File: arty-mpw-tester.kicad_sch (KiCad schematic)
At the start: 111 parts, among them J1 USB4105-GF-A, J10 61300211121, J11 61300211121, J12 61300211121, J14 61300311121, J15 61300311121, J18 61300411121, J19 61300711121, J20 61300411121, J3 arty_chipKIT_connector, J4 61300211121, J5 61300311121, J6 61300211121, J7 61300211121, J8 61300211121, J9 61300211121, Q1 DTC014TEBTL, SW1 JS202011JCQN, SW3 JS202011JCQN, U1 TAR5S33UTE85LF, U10 TPD4E02B04DQA, U2 FT4232H-56Q, U4 MAX811REUS+T, U5 NTS0102DP, U6 MCP4661-103E/ML, U7 Caravel_breakout_PCB_flexypin, U8 W25Q32FVSS, U9 MIC2211-AAYML-TR, Y1 ABM8G-12.000MHZ-18-D2Y-T, Y2 ECS-2520MVLC-100-BN-TR

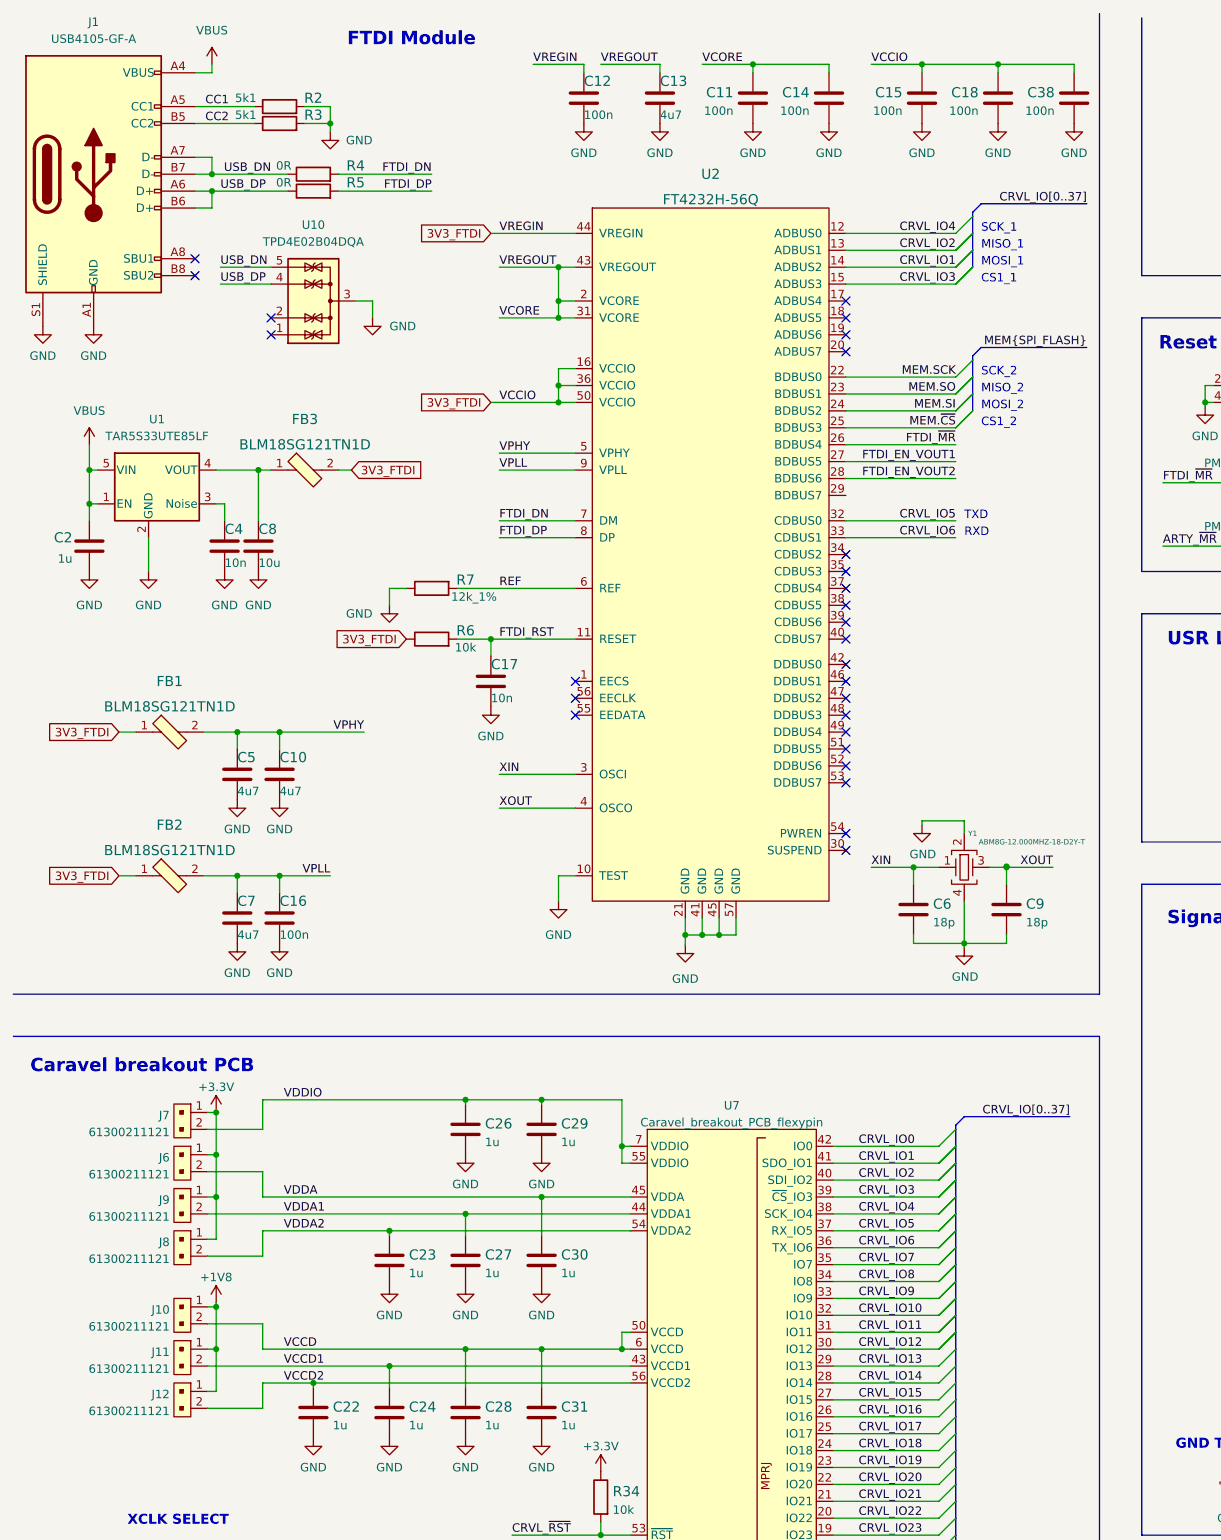
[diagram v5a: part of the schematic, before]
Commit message: Added current monitor schematics. Moved FTDI module to separate subsheet
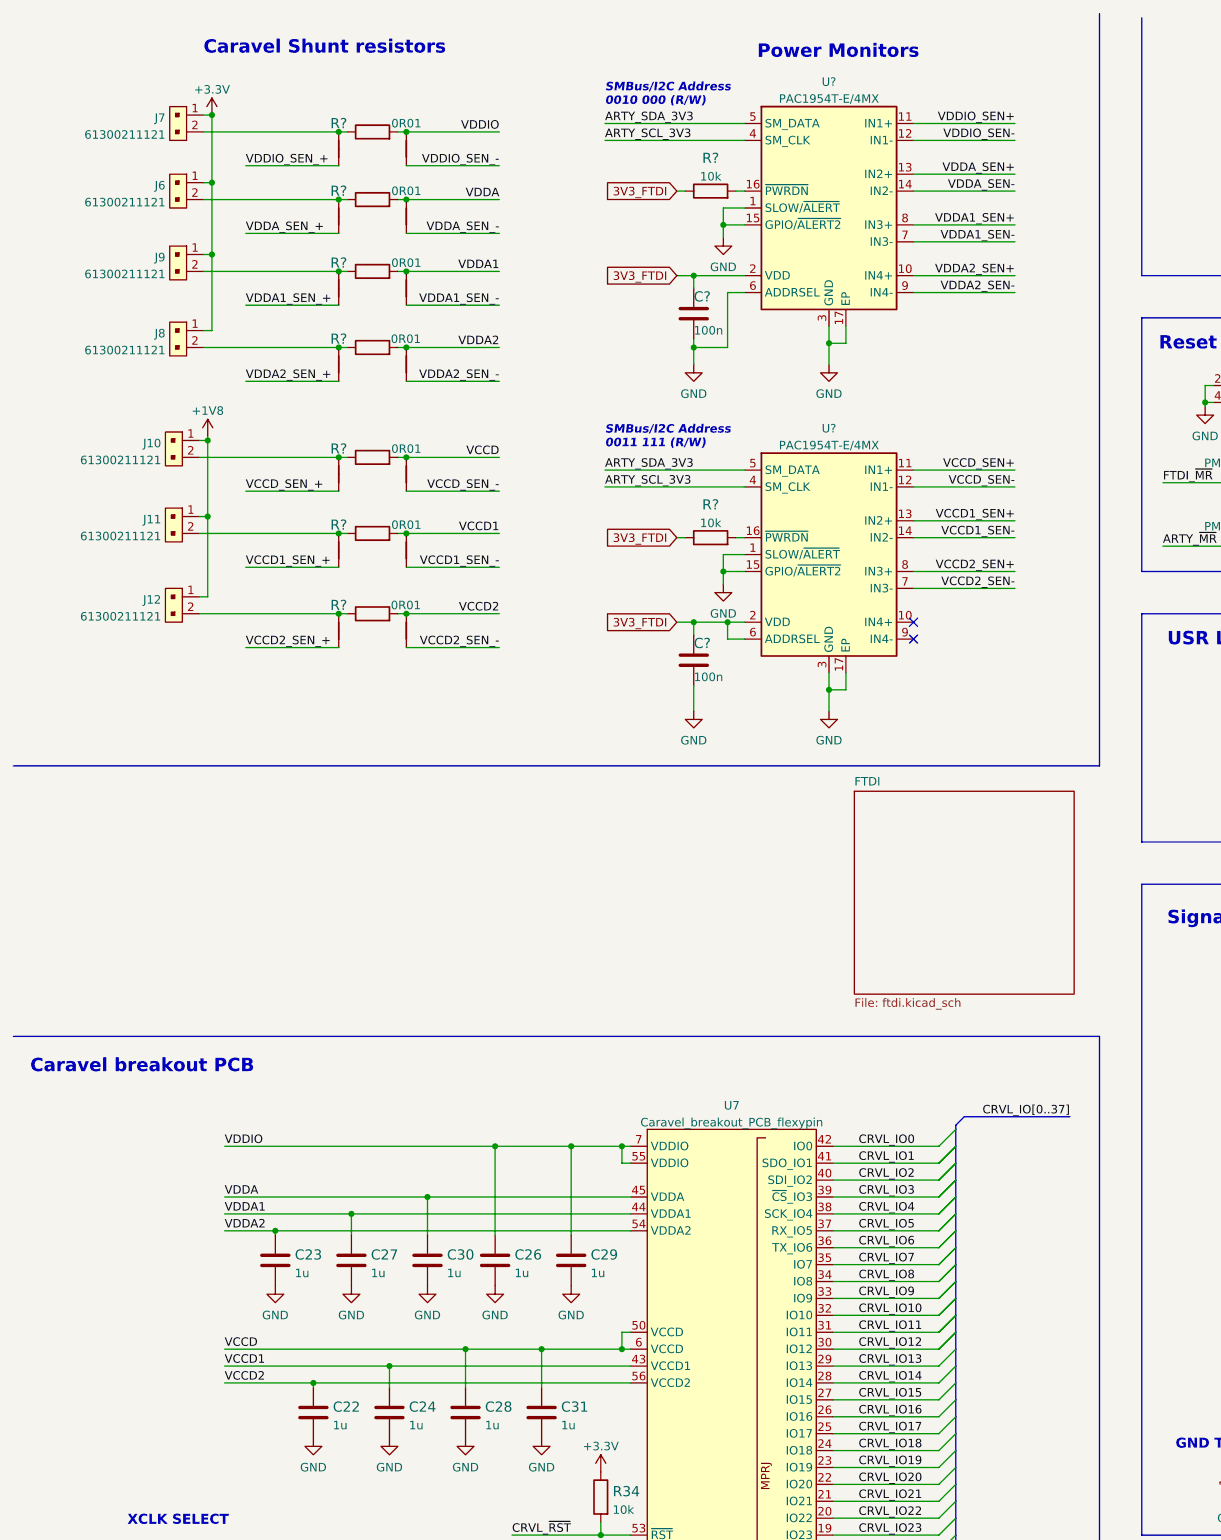
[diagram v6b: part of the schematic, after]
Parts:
- removed C10, C13, C5, C7: C_4u7_0603, arty-mpw-tester-footprints:0603-cap, symbol arty-mpw-tester:C_4u7_0603
- removed C11, C12, C14, C15, C16, C18, C38: C_100n_0603, arty-mpw-tester-footprints:0603-cap, symbol arty-mpw-tester:C_100n_0603
- removed C17, C4: C_10n_0603, arty-mpw-tester-footprints:0603-cap, symbol arty-mpw-tester:C_10n_0603
- removed C2: C_1u_0603, arty-mpw-tester-footprints:0603-cap, symbol arty-mpw-tester:C_1u_0603
- removed C6, C9: C_18p_0603, arty-mpw-tester-footprints:0603-cap, symbol arty-mpw-tester:C_18p_0603
- removed C8: C_10u_0603, antmicro-footprints:0603-cap, symbol antmicroCapacitors0603:C_10u_0603
- removed FB1, FB2, FB3: BLM18SG121TN1D, antmicro-footprints:0603-res, symbol antmicroFerriteBeadsandChips:BLM18SG121TN1D
- removed J1: USB4105-GF-A, arty-mpw-tester-footprints:GCT_USB4105-GF-A, symbol arty-mpw-tester:USB4105-GF-A
- removed R2, R3: R_5k1_0603, arty-mpw-tester-footprints:0603-res, symbol arty-mpw-tester:R_5k1_0603
- removed R4, R5: R_0R_0402, arty-mpw-tester-footprints:0402-res, symbol arty-mpw-tester:R_0R_0402
- removed R6: R_10k_0603, arty-mpw-tester-footprints:0603-res, symbol arty-mpw-tester:R_10k_0603
- removed R7: R_12k_1%_0603, arty-mpw-tester-footprints:0603-res, symbol arty-mpw-tester:R_12k_1%_0603
- removed U1: TAR5S33UTE85LF, antmicro-footprints:SOT-353, symbol antmicroPMICVoltageRegulatorsLinear:TAR5S33UTE85LF
- removed U10: TPD4E02B04DQA, arty-mpw-tester-footprints:USON-10_2.5x1.0mm_P0.5mm, symbol arty-mpw-tester:TPD4E02B04DQA
- removed U2: FT4232H-56Q, antmicro-footprints:QFN-56-1EP_8x8mm_P0.5mm_EP5.5.9x5.9mm, symbol antmicroInterfaceControllers:FT4232H-56Q
- removed Y1: ABM8G-12.000MHZ-18-D2Y-T, arty-mpw-tester-footprints:KX-7, symbol arty-mpw-tester:ABM8G-12.000MHZ-18-D2Y-T
- added C? (x2): C_100n_0603, arty-mpw-tester-footprints:0603-cap, symbol arty-mpw-tester:C_100n_0603
- added NT? (x14): NetTie_2, antmicro-footprints:NetTie-2_SMD_Pad0.127mm, symbol antmicroShuntsJumpers:NetTie_2
- added R? (x7): R_0R01_1206, antmicro-footprints:1206-res, symbol antmicroResistorsmisc:R_0R01_1206
- added R? (x2): R_10k_0603, arty-mpw-tester-footprints:0603-res, symbol arty-mpw-tester:R_10k_0603
- added U? (x2): PAC1954T-E/4MX, antmicro-footprints:VQFN-16-1EP_3x3mm_P0.5mm_EP1.1x1.1mm, symbol antmicroMicrocontrollers:PAC1954T-E/4MX
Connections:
- net 3V3_FTDI: now also C?.1, C?.1, R?.1, R?.1, U?.2 (VDD), U?.2 (VDD), U?.6 (ADDRSEL)
- net ARTY_SCL_3V3: now also U?.4 (SM_CLK), U?.4 (SM_CLK)
- net ARTY_SDA_3V3: now also U?.5 (SM_DATA), U?.5 (SM_DATA)
- net EP: now also C?.2, C?.2, U?.1 (SLOW/~{ALERT}), U?.1 (SLOW/~{ALERT}), U?.15 (GPIO/~{ALERT2}), U?.15 (GPIO/~{ALERT2}), U?.17 (EP), U?.17 (EP), U?.3 (GND), U?.3 (GND), U?.6 (ADDRSEL)
- net VCCD: now also NT?.2, R?.2; no longer J10.2
- net VCCD1: now also NT?.2, R?.2; no longer J11.2
- net VCCD2: now also NT?.2, R?.2; no longer J12.2
- net VDDA: now also NT?.2, R?.2; no longer J6.2
- net VDDA1: now also NT?.2, R?.2; no longer J9.2
- net VDDA2: now also NT?.2, R?.2; no longer J8.2
- net VDDIO: now also NT?.2, R?.2; no longer J7.2
- new net: J8.2, NT?.2, R?.1
- new net: J7.2, NT?.2, R?.1
- new net: J6.2, NT?.2, R?.1
- new net: J9.2, NT?.2, R?.1
- new net: J10.2, NT?.2, R?.1
- new net: R?.2, U?.16 (~{PWRDN}) (x2)
- new net: J12.2, NT?.2, R?.1
- new net: J11.2, NT?.2, R?.1
- new net VCCD1_SEN+: U?.13 (IN2+)
- new net VCCD1_SEN-: U?.14 (IN2-)
- new net VCCD1_SEN_+: NT?.1
- new net VCCD1_SEN_-: NT?.1
- new net VCCD2_SEN+: U?.8 (IN3+)
- new net VCCD2_SEN-: U?.7 (IN3-)
- new net VCCD2_SEN_+: NT?.1
- new net VCCD2_SEN_-: NT?.1
- new net VCCD_SEN+: U?.11 (IN1+)
- new net VCCD_SEN-: U?.12 (IN1-)
- new net VCCD_SEN_+: NT?.1
- new net VCCD_SEN_-: NT?.1
- new net VDDA1_SEN+: U?.8 (IN3+)
- new net VDDA1_SEN-: U?.7 (IN3-)
- new net VDDA1_SEN_+: NT?.1
- new net VDDA1_SEN_-: NT?.1
- new net VDDA2_SEN+: U?.10 (IN4+)
- new net VDDA2_SEN-: U?.9 (IN4-)
- new net VDDA2_SEN_+: NT?.1
- new net VDDA2_SEN_-: NT?.1
- new net VDDA_SEN+: U?.13 (IN2+)
- new net VDDA_SEN-: U?.14 (IN2-)
- new net VDDA_SEN_+: NT?.1
- new net VDDA_SEN_-: NT?.1
- new net VDDIO_SEN+: U?.11 (IN1+)
- new net VDDIO_SEN-: U?.12 (IN1-)
- new net VDDIO_SEN_+: NT?.1
- new net VDDIO_SEN_-: NT?.1
- no-connect marks 37 -> 12
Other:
- added sheet FTDI (ftdi.kicad_sch)
- note added: "Caravel Shunt resistors"
- note added: "Power Monitors"
- note added: "SMBus/I2C Address 0010 000 (R/W)"
- note added: "SMBus/I2C Address 0011 111 (R/W)"
- note removed: "CS1_1"
- note removed: "CS1_2"
- note removed: "FTDI Module"
- note removed: "MISO_1"
- note removed: "MISO_2"
- note removed: "MOSI_1"
- note removed: "MOSI_2"
- note removed: "RXD"
- note removed: "SCK_1"
- note removed: "SCK_2"
- note removed: "TXD"
- moved on the sheet: C23, C26, C27, C29, C30, J10, J11, J12, J6, J7, J8, J9

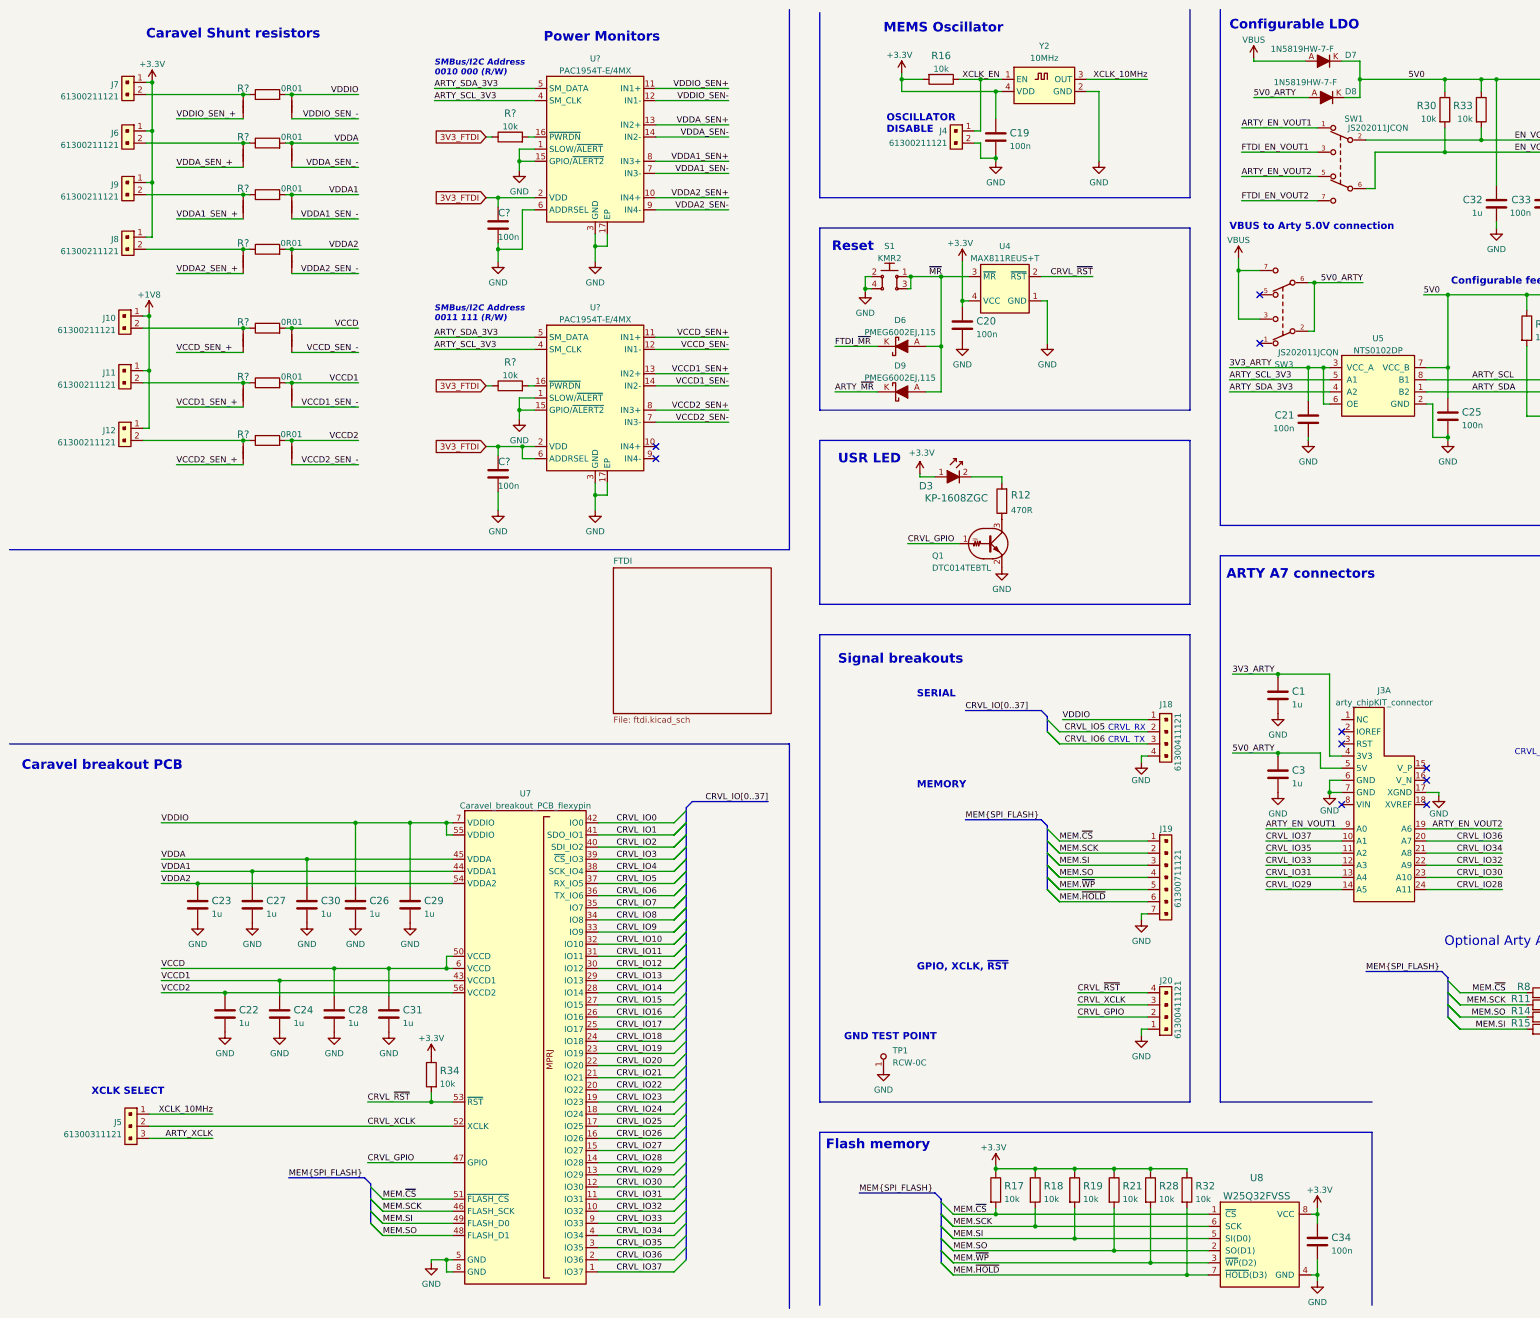
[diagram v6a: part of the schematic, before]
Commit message: Adjusted net naming to work in subsheet
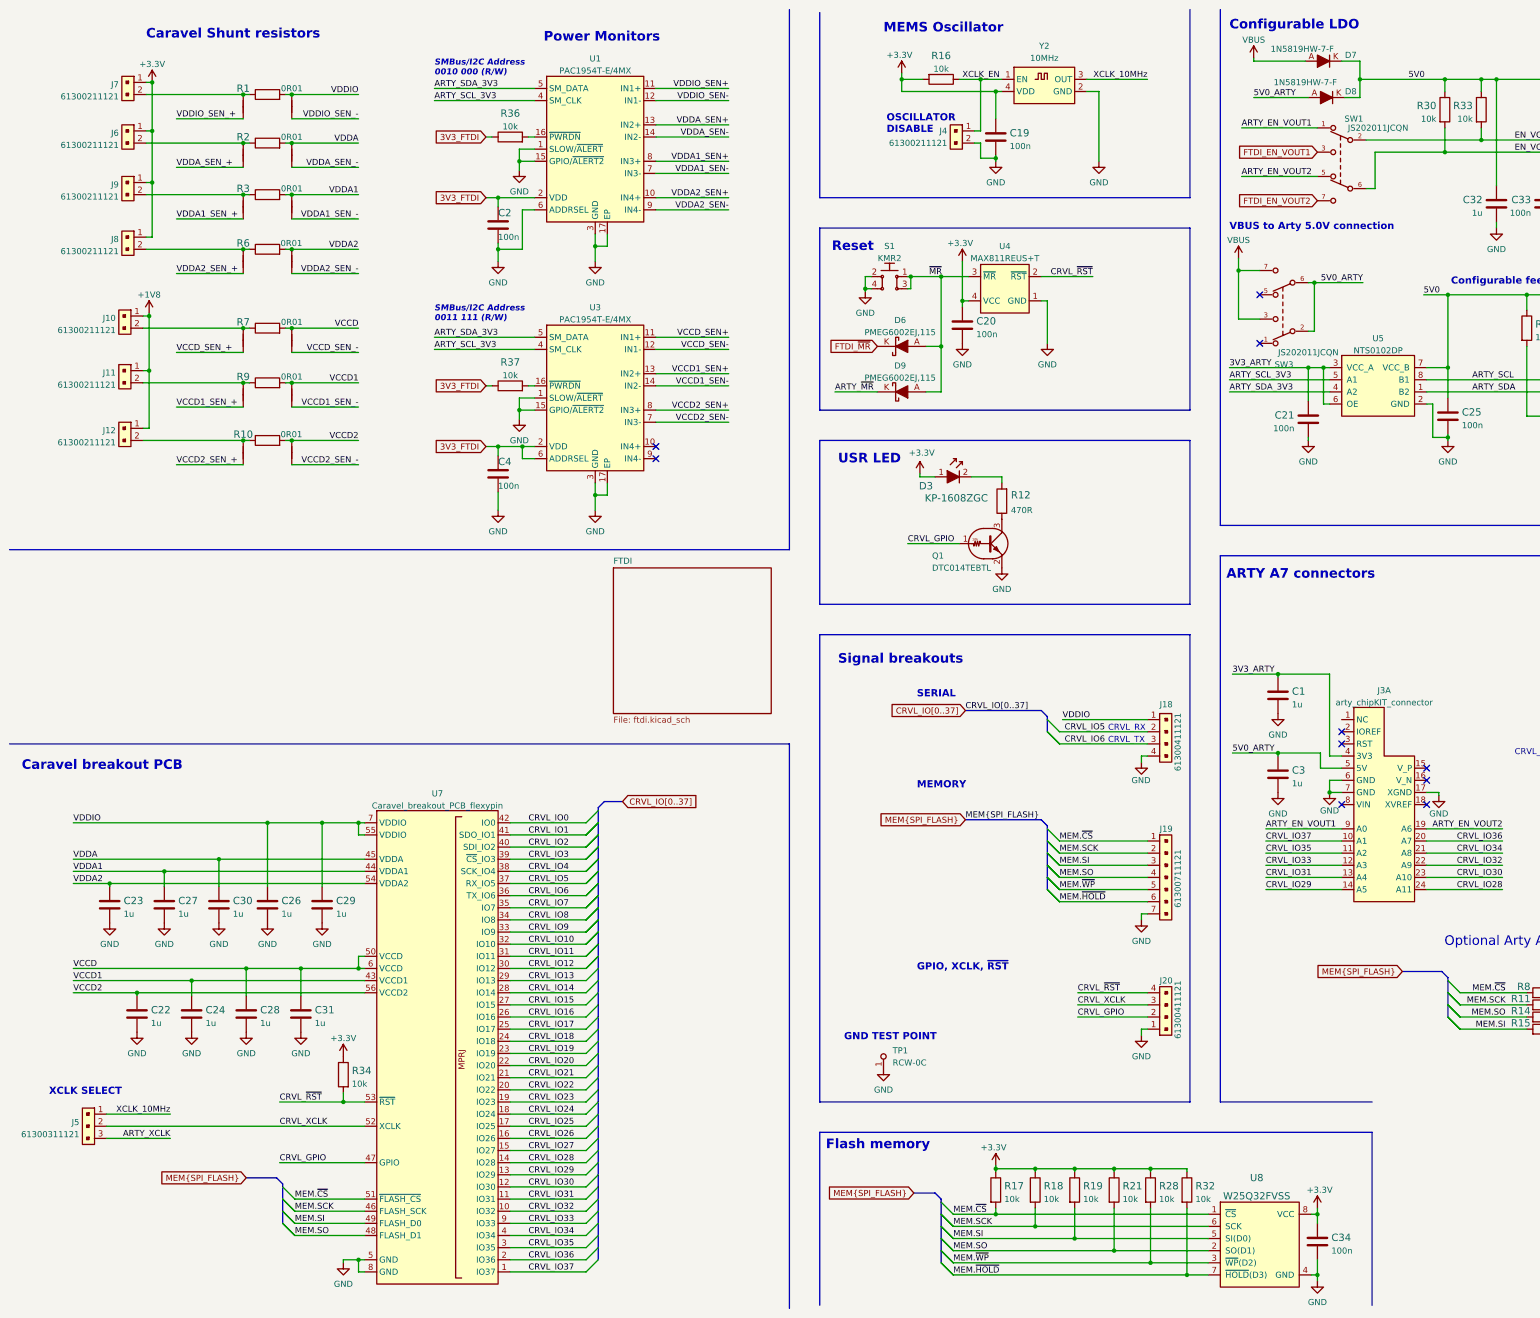
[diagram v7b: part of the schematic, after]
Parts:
- gave numbers to parts that had none: 27
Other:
- moved on the sheet: C22, C23, C24, C26, C27, C28, C29, C30, C31, J5, R34, U7
